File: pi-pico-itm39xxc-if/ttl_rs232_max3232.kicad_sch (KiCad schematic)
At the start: 13 parts

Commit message: Working on pico itm interface
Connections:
- net Vcc renamed Vdd
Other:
- note added: "Supply info - Input voltage (Vdd): 3 V - 5.5 V Design notes [1] These resistors are placed right after the signal drive to provide some kind of damping in case the line is too long. [2] No pull-down resistors are placed here because, according to MAX3232's datasheet, the inputs already have pull-down resistors. [3] Pull-down resistors are placed here in order to prevent the transmitters to float.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"
- note removed: "Supply info - Input voltage (Vcc): 3 V - 5.5 V Design notes [1] These resistors are placed right after the signal drive to provide some kind of damping in case the line is too long. [2] No pull-down resistors are placed here because, according to MAX3232's datasheet, the inputs already have pull-down resistors. [3] Pull-down resistors are placed here in order to prevent the transmitters to float.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"
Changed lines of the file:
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@@
     (effects (font (size 1.27 1.27)) (justify left bottom))
   )
-  (text "Supply info\n - Input voltage (Vcc): 3 V - 5.5 V\n\nDesign notes\n\n[1] These resistors are placed right after the signal drive to\nprovide some kind of damping in case the line is too long.\n\n[2] No pull-down resistors are placed here because, according\nto MAX3232's datasheet, the inputs already have pull-down \nresistors.\n\n[3] Pull-down resistors are placed here in order to prevent the\ntransmitters to float.\n\n[4] These resistors would not be necessary if the host controller\nis on the same PCB. However, assuming that we'll maybe use this\nboard with some jumper cables, we place these resistors here.\n\nTODO\n - Add LEDs on RX/TX lines? Which ones?"
+  (text "Supply info\n - Input voltage (Vdd): 3 V - 5.5 V\n\nDesign notes\n\n[1] These resistors are placed right after the signal drive to\nprovide some kind of damping in case the line is too long.\n\n[2] No pull-down resistors are placed here because, according\nto MAX3232's datasheet, the inputs already have pull-down \nresistors.\n\n[3] Pull-down resistors are placed here in order to prevent the\ntransmitters to float.\n\n[4] These resistors would not be necessary if the host controller\nis on the same PCB. However, assuming that we'll maybe use this\nboard with some jumper cables, we place these resistors here.\n\nTODO\n - Add LEDs on RX/TX lines? Which ones?"
     (at 121.92 59.944 0)
     (effects (font (size 1.27 1.27)) (justify left bottom))
@@
     (effects (font (size 1.27 1.27)) (justify right bottom))
   )
-  (label "Vcc" (at 23.622 98.552 180)
+  (label "Vdd" (at 23.622 98.552 180)
     (effects (font (size 1.27 1.27)) (justify right bottom))
   )
@@
     (effects (font (size 1.27 1.27)) (justify right bottom))
   )
-  (label "Vcc" (at 48.26 18.542 180)
+  (label "Vdd" (at 48.26 18.542 180)
     (effects (font (size 1.27 1.27)) (justify right bottom))
   )
@@
     (effects (font (size 1.27 1.27)) (justify left))
   )
-  (hierarchical_label "Vcc" (shape input) (at 26.162 98.552 0)
+  (hierarchical_label "Vdd" (shape input) (at 26.162 98.552 0)
     (effects (font (size 1.27 1.27)) (justify left))
   )

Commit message: Passing ERC
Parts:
- gave numbers to parts that had none: 13
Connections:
- net RX1_232 is gone; now on net RX1_RS232: U3.13 (R1IN)
- net RX2_232 is gone; now on net RX2_RS232: U3.8 (R2IN)
- net TX1_232 is gone; now on net TX1_RS232: R11.1
- net TX2_232 is gone; now on net TX2_RS232: R12.1
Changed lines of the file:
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@@
     (effects (font (size 1.27 1.27)) (justify right bottom))
   )
-  (label "TX2_232" (at 94.742 62.738 0)
+  (label "TX2_RS232" (at 94.742 62.738 0)
     (effects (font (size 1.27 1.27)) (justify left bottom))
   )
@@
     (effects (font (size 1.27 1.27)) (justify right bottom))
   )
-  (label "TX1_232" (at 94.742 57.658 0)
+  (label "TX1_RS232" (at 94.742 57.658 0)
     (effects (font (size 1.27 1.27)) (justify left bottom))
   )
@@
     (effects (font (size 1.27 1.27)) (justify right bottom))
   )
-  (label "RX2_232" (at 94.996 72.898 0)
-    (effects (font (size 1.27 1.27)) (justify left bottom))
-  )
-  (label "RX1_232" (at 94.742 67.818 0)
+  (label "RX2_RS232" (at 94.996 72.898 0)
+    (effects (font (size 1.27 1.27)) (justify left bottom))
+  )
+  (label "RX1_RS232" (at 94.742 67.818 0)
     (effects (font (size 1.27 1.27)) (justify left bottom))
   )
@@
   (symbol (lib_id "Device:C_Small") (at 45.212 36.068 0) (mirror y) (unit 1)
     (in_bom yes) (on_board yes)
-    (property "Reference" "C?" (id 0) (at 43.18 34.798 0)
+    (property "Reference" "C12" (id 0) (at 43.18 34.798 0)
       (effects (font (size 1.27 1.27)) (justify left))
     )
@@
   (symbol (lib_id "Device:C_Small") (at 58.42 22.352 0) (unit 1)
     (in_bom yes) (on_board yes)
-    (property "Reference" "C?" (id 0) (at 60.452 21.082 0)
+    (property "Reference" "C11" (id 0) (at 60.452 21.082 0)
       (effects (font (size 1.27 1.27)) (justify left))
     )
@@
   (symbol (lib_id "Device:C_Small") (at 88.392 36.068 0) (unit 1)
     (in_bom yes) (on_board yes)
-    (property "Reference" "C?" (id 0) (at 90.424 34.798 0)
+    (property "Reference" "C13" (id 0) (at 90.424 34.798 0)
       (effects (font (size 1.27 1.27)) (justify left))
     )
@@
   (symbol (lib_id "Device:R_Small") (at 42.672 72.898 270) (unit 1)
     (in_bom yes) (on_board yes)
-    (property "Reference" "R?" (id 0) (at 42.672 71.12 90))
+    (property "Reference" "R14" (id 0) (at 42.672 71.12 90))
     (property "Value" "47R" (id 1) (at 42.672 74.676 90))
     (property "Footprint" "Resistor_SMD:R_0805_2012Metric_Pad1.20x1.40mm_HandSolder" (id 2) (at 42.672 72.898 0)
@@
   (symbol (lib_id "Device:R_Small") (at 45.466 53.848 0) (unit 1)
     (in_bom yes) (on_board yes)
-    (property "Reference" "R?" (id 0) (at 43.18 52.578 0))
+    (property "Reference" "R10" (id 0) (at 43.18 52.578 0))
     (property "Value" "10k" (id 1) (at 42.418 54.864 0))
     (property "Footprint" "Resistor_SMD:R_0805_2012Metric_Pad1.20x1.40mm_HandSolder" (id 2) (at 45.466 53.848 0)
@@
   (symbol (lib_id "Device:R_Small") (at 90.932 57.658 270) (unit 1)
     (in_bom yes) (on_board yes)
-    (property "Reference" "R?" (id 0) (at 90.932 55.88 90))
+    (property "Reference" "R11" (id 0) (at 90.932 55.88 90))
     (property "Value" "47R" (id 1) (at 90.932 59.436 90))
     (property "Footprint" "Resistor_SMD:R_0805_2012Metric_Pad1.20x1.40mm_HandSolder" (id 2) (at 90.932 57.658 0)
@@
   (symbol (lib_id "Device:R_Small") (at 39.37 53.848 0) (unit 1)
     (in_bom yes) (on_board yes)
-    (property "Reference" "R?" (id 0) (at 37.084 52.578 0))
+    (property "Reference" "R9" (id 0) (at 37.084 52.578 0))
     (property "Value" "10k" (id 1) (at 36.322 54.864 0))
     (property "Footprint" "Resistor_SMD:R_0805_2012Metric_Pad1.20x1.40mm_HandSolder" (id 2) (at 39.37 53.848 0)
@@
   (symbol (lib_id "Interface_UART:MAX3232") (at 66.802 55.118 0) (unit 1)
     (in_bom yes) (on_board yes) (fields_autoplaced)
-    (property "Reference" "U?" (id 0) (at 68.8214 23.876 0)
+    (property "Reference" "U3" (id 0) (at 68.8214 23.876 0)
       (effects (font (size 1.27 1.27)) (justify left))
     )
@@
   (symbol (lib_id "Device:R_Small") (at 90.932 62.738 270) (unit 1)
     (in_bom yes) (on_board yes)
-    (property "Reference" "R?" (id 0) (at 90.932 60.96 90))
+    (property "Reference" "R12" (id 0) (at 90.932 60.96 90))
     (property "Value" "47R" (id 1) (at 90.932 64.516 90))
     (property "Footprint" "Resistor_SMD:R_0805_2012Metric_Pad1.20x1.40mm_HandSolder" (id 2) (at 90.932 62.738 0)
@@
   (symbol (lib_id "Device:C_Small") (at 91.186 44.958 90) (mirror x) (unit 1)
     (in_bom yes) (on_board yes)
-    (property "Reference" "C?" (id 0) (at 90.17 43.688 90)
+    (property "Reference" "C14" (id 0) (at 90.17 43.688 90)
       (effects (font (size 1.27 1.27)) (justify left))
     )
@@
   (symbol (lib_id "Device:C_Small") (at 91.186 52.578 90) (mirror x) (unit 1)
     (in_bom yes) (on_board yes)
-    (property "Reference" "C?" (id 0) (at 90.17 51.308 90)
+    (property "Reference" "C15" (id 0) (at 90.17 51.308 90)
       (effects (font (size 1.27 1.27)) (justify left))
     )
@@
   (symbol (lib_id "Device:R_Small") (at 42.672 67.818 270) (unit 1)
     (in_bom yes) (on_board yes)
-    (property "Reference" "R?" (id 0) (at 42.672 66.04 90))
+    (property "Reference" "R13" (id 0) (at 42.672 66.04 90))
     (property "Value" "47R" (id 1) (at 42.672 69.596 90))
     (property "Footprint" "Resistor_SMD:R_0805_2012Metric_Pad1.20x1.40mm_HandSolder" (id 2) (at 42.672 67.818 0)
@@
   (symbol (lib_id "Device:C_Small") (at 49.53 22.352 0) (unit 1)
     (in_bom yes) (on_board yes)
-    (property "Reference" "C?" (id 0) (at 51.562 21.082 0)
-      (effects (font (size 1.27 1.27)) (justify left))
-    )
+    (property "Reference" "C10" (id 0) (at 51.562 21.082 0)
+      (effects (font (size 1.27 1.27)) (justify left))
+    )

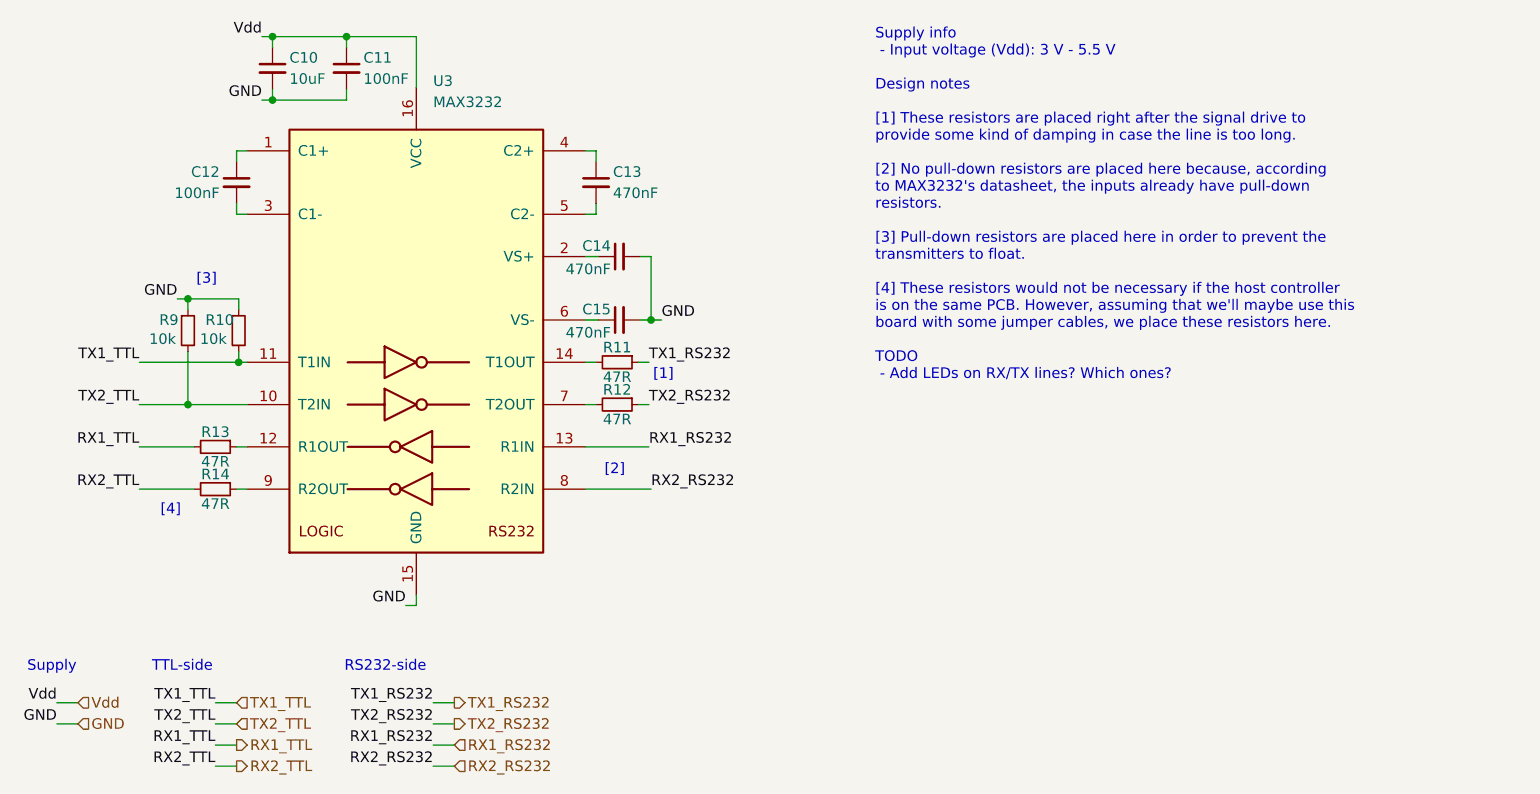
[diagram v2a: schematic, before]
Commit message: Working on pcb for pi pico it
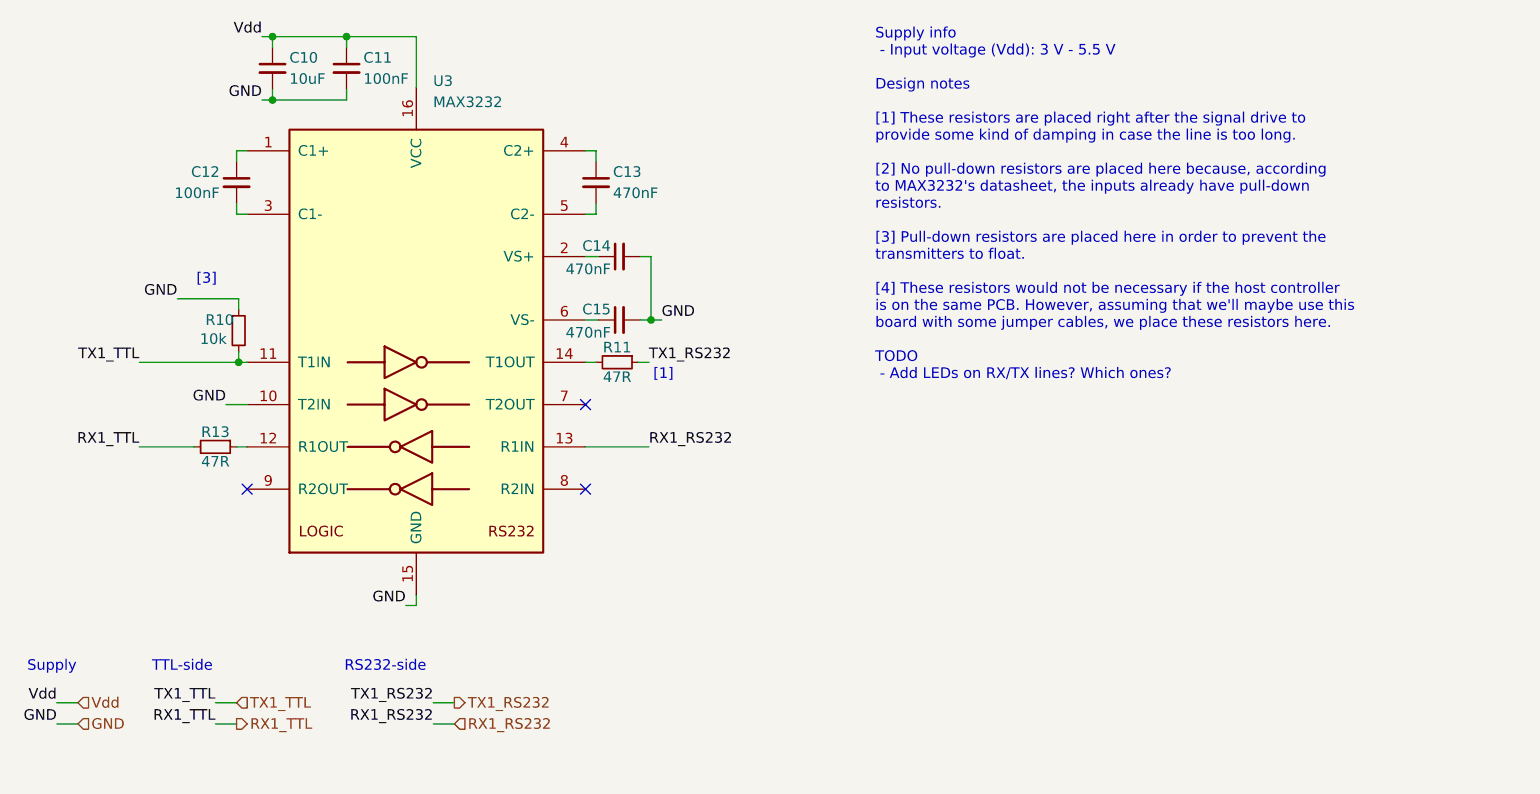
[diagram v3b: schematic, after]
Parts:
- removed R12, R14: 47R, Resistor_SMD:R_0805_2012Metric_Pad1.20x1.40mm_HandSolder, symbol Device:R_Small
- removed R9: 10k, Resistor_SMD:R_0805_2012Metric_Pad1.20x1.40mm_HandSolder, symbol Device:R_Small
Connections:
- net TX2_TTL is gone; now on net GND: U3.10 (T2IN)
- net RX2_RS232: no longer names the net of U3.8 (R2IN)
- no-connect marks 0 -> 3
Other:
- note removed: "[2]"
- note removed: "[4]"
